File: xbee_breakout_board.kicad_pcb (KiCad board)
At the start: 2 copper layers, 40.1 x 30 mm, 4 parts, among them J1 Conn_01x10_Male, J2 Conn_01x10_Female, J3 Conn_01x10_Male, J4 Conn_01x10_Female

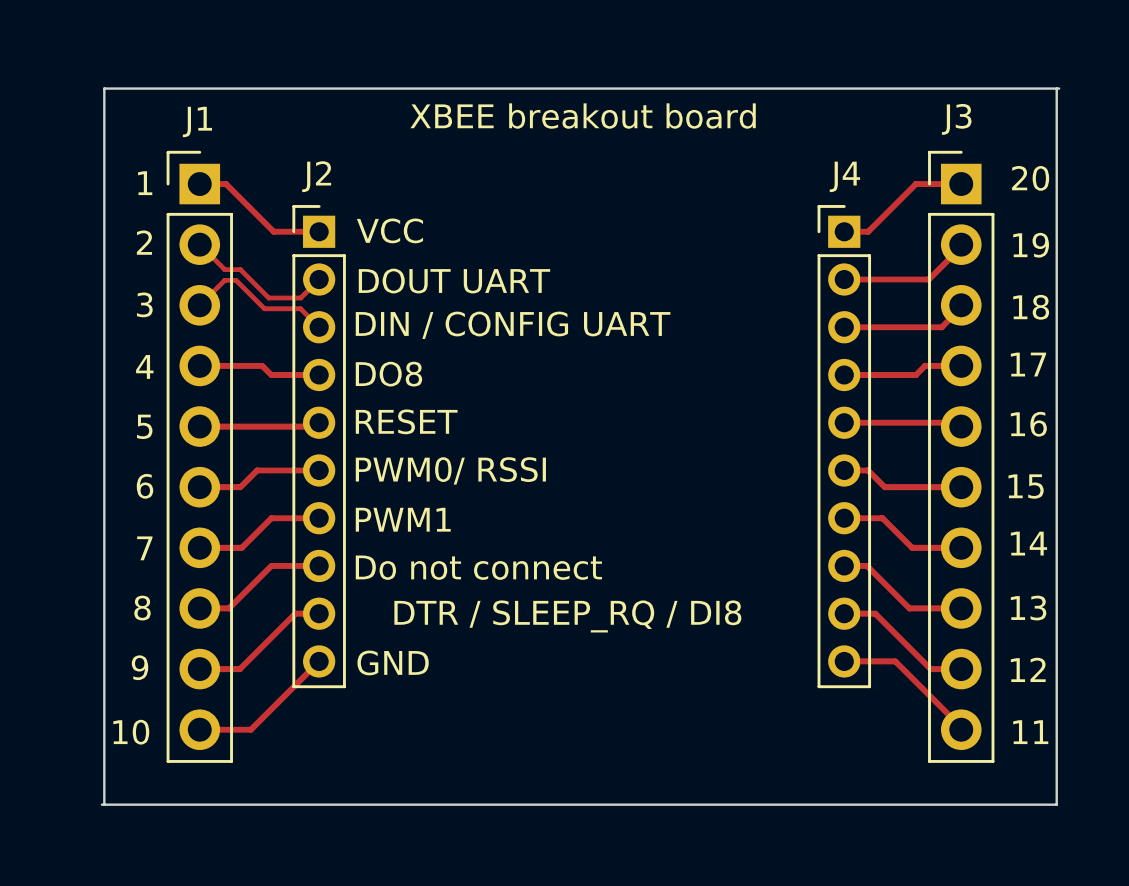
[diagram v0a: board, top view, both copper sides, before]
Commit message: fix error in design
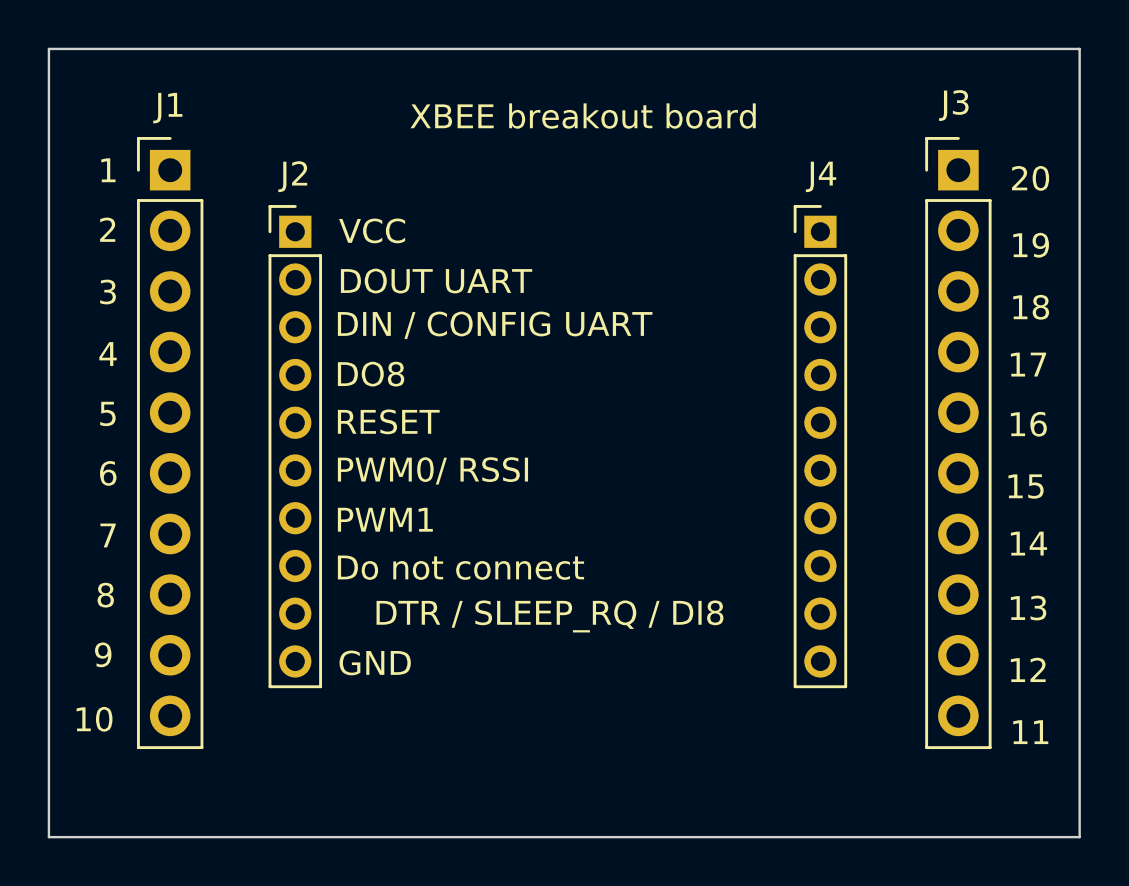
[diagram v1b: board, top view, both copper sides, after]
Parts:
- moved J1 1.37 mm to (111.8, 58.4)
- moved J2 1.00 mm to (117.0, 61.0)
- moved J4 1.00 mm to (139.0, 61.0)
- moved J3 0.59 mm to (144.8, 58.4)
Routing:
- net /D-: track 6.25 -> 0.00 mm
- net /D+: track 6.25 -> 0.00 mm
- net Net-(J1-Pad10): track 6.18 -> 0.00 mm
- net Net-(J3-Pad10): track 6.18 -> 0.00 mm
- net Net-(J3-Pad9): track 5.96 -> 0.00 mm
- net Net-(J1-Pad9): track 5.96 -> 0.00 mm
- net Net-(J3-Pad1): track 5.83 -> 0.00 mm
- net Net-(J1-Pad1): track 5.83 -> 0.00 mm
- net Net-(J3-Pad8): track 5.74 -> 0.00 mm
- net Net-(J1-Pad8): track 5.74 -> 0.00 mm
- net Net-(J3-Pad2): track 5.60 -> 0.00 mm
- net Net-(J1-Pad7): track 5.51 -> 0.00 mm
- net Net-(J3-Pad7): track 5.51 -> 0.00 mm
- net Net-(J3-Pad3): track 5.38 -> 0.00 mm
- net Net-(J3-Pad6): track 5.29 -> 0.00 mm
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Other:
- board size 40.1 x 30 mm -> 43.2 x 33 mm

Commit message: add traced back to top layer
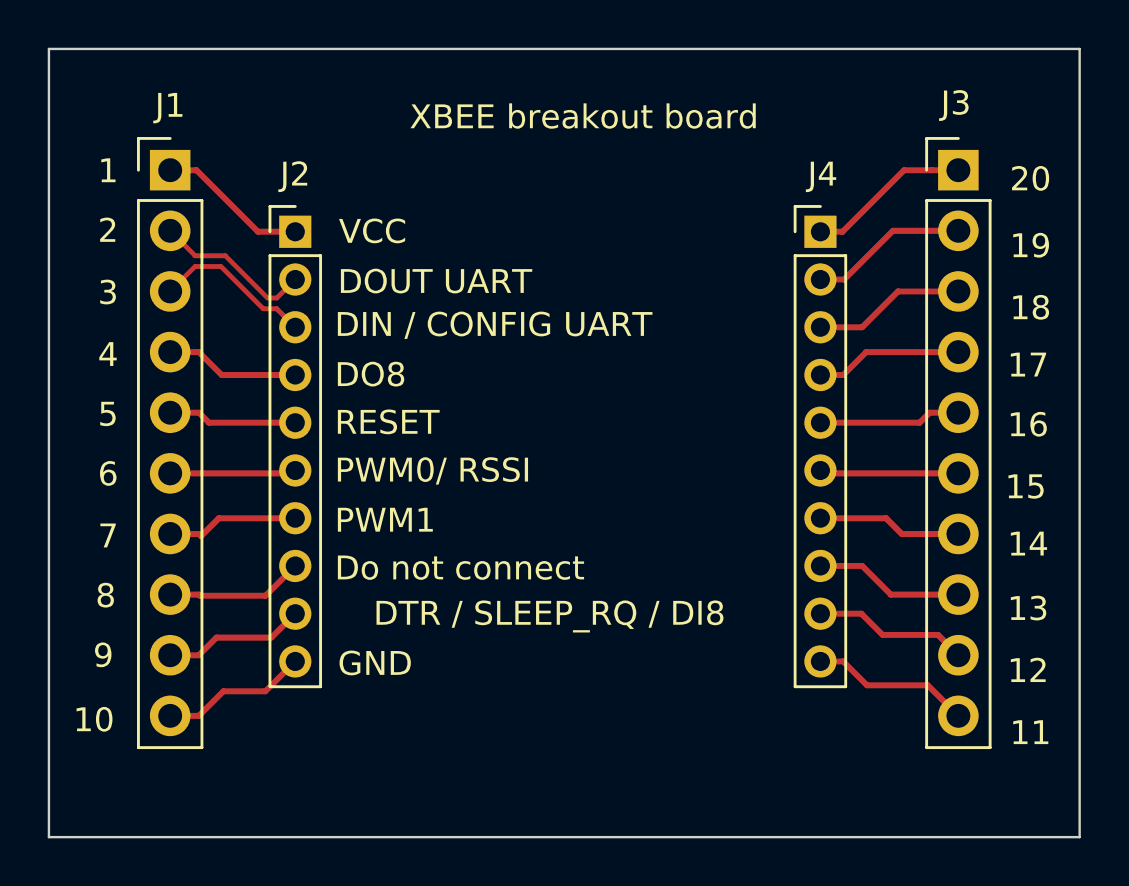
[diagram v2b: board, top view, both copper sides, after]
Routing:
- net Net-(J3-Pad1): track 0.00 -> 6.85 mm
- net /D-: track 0.00 -> 6.73 mm
- net /D+: track 0.00 -> 6.73 mm
- net Net-(J3-Pad10): track 0.00 -> 6.72 mm
- net Net-(J3-Pad2): track 0.00 -> 6.62 mm
- net Net-(J3-Pad9): track 0.00 -> 6.50 mm
- net Net-(J3-Pad3): track 0.00 -> 6.40 mm
- net Net-(J1-Pad1): track 0.00 -> 6.31 mm
- net Net-(J3-Pad8): track 0.00 -> 6.28 mm
- net Net-(J1-Pad10): track 0.00 -> 6.18 mm
- net Net-(J3-Pad4): track 0.00 -> 6.18 mm
- net Net-(J3-Pad7): track 0.00 -> 6.05 mm
- net Net-(J1-Pad9): track 0.00 -> 5.96 mm
- net Net-(J3-Pad5): track 0.23 -> 6.18 mm
- net Net-(J3-Pad6): track 0.00 -> 5.83 mm
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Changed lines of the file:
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@@
     (thickness 1.6)
     (drawings 66)
-    (tracks 2)
+    (tracks 71)
     (zones 0)
     (modules 4)
@@
     (34 B.Paste user)
     (35 F.Paste user)
-    (36 B.SilkS user hide)
+    (36 B.SilkS user)
     (37 F.SilkS user)
     (38 B.Mask user)
@@
     (effects (font (size 1 1) (thickness 0.15)))
   )
+  (segment (start 115.44 61) (end 117 61) (width 0.25) (layer F.Cu) (net 1))
+  (segment (start 111.76 58.42) (end 112.86 58.42) (width 0.25) (layer F.Cu) (net 1))
+  (segment (start 112.86 58.42) (end 115.44 61) (width 0.25) (layer F.Cu) (net 1))
+  (segment (start 113.922081 67) (end 117 67) (width 0.25) (layer F.Cu) (net 2))
+  (segment (start 111.76 66.04) (end 112.962081 66.04) (width 0.25) (layer F.Cu) (net 2))
+  (segment (start 112.962081 66.04) (end 113.922081 67) (width 0.25) (layer F.Cu) (net 2))
   (segment (start 116.84 69.16) (end 117 69) (width 0.25) (layer F.Cu) (net 3))
+  (segment (start 112.962081 68.58) (end 113.382081 69) (width 0.25) (layer F.Cu) (net 3))
+  (segment (start 111.76 68.58) (end 112.962081 68.58) (width 0.25) (layer F.Cu) (net 3))
+  (segment (start 113.382081 69) (end 117 69) (width 0.25) (layer F.Cu) (net 3))
+  (segment (start 116.88 71.12) (end 117 71) (width 0.25) (layer F.Cu) (net 4))
+  (segment (start 111.76 71.12) (end 116.88 71.12) (width 0.25) (layer F.Cu) (net 4))
+  (segment (start 112.962081 73.66) (end 113.052081 73.75) (width 0.25) (layer F.Cu) (net 5))
+  (segment (start 111.76 73.66) (end 112.962081 73.66) (width 0.25) (layer F.Cu) (net 5))
+  (segment (start 113.802081 73) (end 117 73) (width 0.25) (layer F.Cu) (net 5))
+  (segment (start 113.052081 73.75) (end 113.802081 73) (width 0.25) (layer F.Cu) (net 5))
+  (segment (start 112.962081 76.2) (end 113.012081 76.25) (width 0.25) (layer F.Cu) (net 6))
+  (segment (start 111.76 76.2) (end 112.962081 76.2) (width 0.25) (layer F.Cu) (net 6))
+  (segment (start 115.75 76.25) (end 117 75) (width 0.25) (layer F.Cu) (net 6))
+  (segment (start 113.012081 76.25) (end 115.75 76.25) (width 0.25) (layer F.Cu) (net 6))
+  (segment (start 112.962081 78.74) (end 113.702081 78) (width 0.25) (layer F.Cu) (net 7))
+  (segment (start 111.76 78.74) (end 112.962081 78.74) (width 0.25) (layer F.Cu) (net 7))
+  (segment (start 116 78) (end 117 77) (width 0.25) (layer F.Cu) (net 7))
+  (segment (start 113.702081 78) (end 116 78) (width 0.25) (layer F.Cu) (net 7))
+  (segment (start 112.962081 81.28) (end 113.992081 80.25) (width 0.25) (layer F.Cu) (net 8))
+  (segment (start 111.76 81.28) (end 112.962081 81.28) (width 0.25) (layer F.Cu) (net 8))
+  (segment (start 115.75 80.25) (end 117 79) (width 0.25) (layer F.Cu) (net 8))
+  (segment (start 113.992081 80.25) (end 115.75 80.25) (width 0.25) (layer F.Cu) (net 8))
+  (segment (start 139.954594 79) (end 140.954594 80) (width 0.25) (layer F.Cu) (net 9))
+  (segment (start 139 79) (end 139.954594 79) (width 0.25) (layer F.Cu) (net 9))
+  (segment (start 143.5 80) (end 144.78 81.28) (width 0.25) (layer F.Cu) (net 9))
+  (segment (start 140.954594 80) (end 143.5 80) (width 0.25) (layer F.Cu) (net 9))
+  (segment (start 143.930001 77.890001) (end 141.609999 77.890001) (width 0.25) (layer F.Cu) (net 10))
+  (segment (start 144.78 78.74) (end 143.930001 77.890001) (width 0.25) (layer F.Cu) (net 10))
+  (segment (start 140.719998 77) (end 139 77) (width 0.25) (layer F.Cu) (net 10))
+  (segment (start 141.609999 77.890001) (end 140.719998 77) (width 0.25) (layer F.Cu) (net 10))
+  (segment (start 144.78 76.2) (end 141.95 76.2) (width 0.25) (layer F.Cu) (net 11))
+  (segment (start 140.75 75) (end 139 75) (width 0.25) (layer F.Cu) (net 11))
+  (segment (start 141.95 76.2) (end 140.75 75) (width 0.25) (layer F.Cu) (net 11))
+  (segment (start 144.78 73.66) (end 142.41 73.66) (width 0.25) (layer F.Cu) (net 12))
+  (segment (start 141.75 73) (end 139 73) (width 0.25) (layer F.Cu) (net 12))
+  (segment (start 142.41 73.66) (end 141.75 73) (width 0.25) (layer F.Cu) (net 12))
+  (segment (start 139.12 71.12) (end 139 71) (width 0.25) (layer F.Cu) (net 13))
+  (segment (start 144.78 71.12) (end 139.12 71.12) (width 0.25) (layer F.Cu) (net 13))
   (segment (start 144.84 69) (end 145 69.16) (width 0.25) (layer F.Cu) (net 14))
+  (segment (start 143.577919 68.58) (end 143.157919 69) (width 0.25) (layer F.Cu) (net 14))
+  (segment (start 144.78 68.58) (end 143.577919 68.58) (width 0.25) (layer F.Cu) (net 14))
+  (segment (start 143.157919 69) (end 139 69) (width 0.25) (layer F.Cu) (net 14))
+  (segment (start 140.914594 66.04) (end 144.78 66.04) (width 0.25) (layer F.Cu) (net 15))
+  (segment (start 139 67) (end 139.954594 67) (width 0.25) (layer F.Cu) (net 15))
+  (segment (start 139.954594 67) (end 140.914594 66.04) (width 0.25) (layer F.Cu) (net 15))
+  (segment (start 140.75 65) (end 139 65) (width 0.25) (layer F.Cu) (net 16))
+  (segment (start 144.78 63.5) (end 142.25 63.5) (width 0.25) (layer F.Cu) (net 16))
+  (segment (start 142.25 63.5) (end 140.75 65) (width 0.25) (layer F.Cu) (net 16))
+  (segment (start 139 63) (end 140 63) (width 0.25) (layer F.Cu) (net 17))
+  (segment (start 142.04 60.96) (end 144.78 60.96) (width 0.25) (layer F.Cu) (net 17))
+  (segment (start 140 63) (end 142.04 60.96) (width 0.25) (layer F.Cu) (net 17))
+  (segment (start 143.68 58.42) (end 144.78 58.42) (width 0.25) (layer F.Cu) (net 18))
+  (segment (start 142.505 58.42) (end 143.68 58.42) (width 0.25) (layer F.Cu) (net 18))
+  (segment (start 139.925 61) (end 142.505 58.42) (width 0.25) (layer F.Cu) (net 18))
+  (segment (start 139 61) (end 139.925 61) (width 0.25) (layer F.Cu) (net 18))
+  (segment (start 111.76 60.96) (end 112.805 62.005) (width 0.2) (layer F.Cu) (net 19))
+  (segment (start 112.805 62.005) (end 114.0732 62.005) (width 0.2) (layer F.Cu) (net 19))
+  (segment (start 115.8432 63.775) (end 116.225 63.775) (width 0.2) (layer F.Cu) (net 19))
+  (segment (start 114.0732 62.005) (end 115.8432 63.775) (width 0.2) (layer F.Cu) (net 19))
+  (segment (start 116.225 63.775) (end 117 63) (width 0.2) (layer F.Cu) (net 19))
+  (segment (start 111.76 63.5) (end 112.805 62.455) (width 0.2) (layer F.Cu) (net 20))
+  (segment (start 112.805 62.455) (end 113.8868 62.455) (width 0.2) (layer F.Cu) (net 20))
+  (segment (start 116.225 64.225) (end 117 65) (width 0.2) (layer F.Cu) (net 20))
+  (segment (start 113.8868 62.455) (end 115.6568 64.225) (width 0.2) (layer F.Cu) (net 20))
+  (segment (start 115.6568 64.225) (end 116.225 64.225) (width 0.2) (layer F.Cu) (net 20))
 )
